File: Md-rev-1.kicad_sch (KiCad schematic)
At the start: 25 parts, among them CN1 JSTPH, J1 USB_C_Receptacle_USB2.0, J2 54-00177, U1 MCP73831-2-OT, U2 MAX9814

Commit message: updated gerberfiles and symbols
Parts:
- removed MK1: Microphone_Condensor, Buzzer_Beeper:MagneticBuzzer_Kobitone_254-EMB73-RO, symbol Device:Microphone_Condenser
- added MK1: CMA-4544PF-W, CMA-4544PF-W:MIC_CMA-4544PF-W, symbol CMA_4544PF_W:CMA-4544PF-W
- renumbered R10 to R9
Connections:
- net GND: now also MK1.1
- net at C5.1, R8.1: now also MK1.2
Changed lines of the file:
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@@
   (junction (at 158.75 121.92) (diameter 0) (color 0 0 0 0)
   )
+  (junction (at 215.9 128.27) (diameter 0) (color 0 0 0 0)
+  )
   (junction (at 347.98 119.38) (diameter 0) (color 0 0 0 0)
   )
@@
   )
   (junction (at 215.9 118.11) (diameter 0) (color 0 0 0 0)
-  )
-  (junction (at 215.9 128.27) (diameter 0) (color 0 0 0 0)
   )
   (no_connect (at 139.7 119.38))
@@
   (no_connect (at 345.44 121.92))
   (no_connect (at 347.98 116.84))
-  (no_connect (at 234.95 110.49))
+  (no_connect (at 233.68 110.49))
   (no_connect (at 345.44 124.46))
   (no_connect (at 351.79 114.3))
@@
     (stroke (width 0) (type default))
   )
-  (wire (pts (xy 196.85 128.27) (xy 199.39 128.27))
+  (wire (pts (xy 205.74 125.73) (xy 212.09 125.73))
     (stroke (width 0) (type default))
   )
@@
     (stroke (width 0) (type default))
   )
-  (wire (pts (xy 234.95 110.49) (xy 240.03 110.49))
+  (wire (pts (xy 233.68 110.49) (xy 240.03 110.49))
     (stroke (width 0) (type default))
   )
@@
     (stroke (width 0) (type default))
   )
+  (wire (pts (xy 215.9 128.27) (xy 215.9 132.08))
+    (stroke (width 0) (type default))
+  )
   (wire (pts (xy 92.71 88.9) (xy 100.33 88.9))
     (stroke (width 0) (type default))
@@
     (stroke (width 0) (type default))
   )
+  (wire (pts (xy 205.74 125.73) (xy 205.74 127))
+    (stroke (width 0) (type default))
+  )
   (wire (pts (xy 180.34 148.59) (xy 180.34 118.11))
     (stroke (width 0) (type default))
@@
     (stroke (width 0) (type default))
   )
-  (wire (pts (xy 209.55 128.27) (xy 215.9 128.27))
-    (stroke (width 0) (type default))
-  )
   (wire (pts (xy 92.71 120.65) (xy 115.57 120.65))
     (stroke (width 0) (type default))
@@
   )
   (wire (pts (xy 227.33 128.27) (xy 227.33 120.65))
+    (stroke (width 0) (type default))
+  )
+  (wire (pts (xy 205.74 132.08) (xy 215.9 132.08))
     (stroke (width 0) (type default))
   )
@@
     )
   )
-  (symbol (lib_id "Device:Microphone_Condenser") (at 204.47 128.27 270) (unit 1)
-    (in_bom yes) (on_board yes) (dnp no) (fields_autoplaced)
-    (property "Reference" "MK1" (at 205.1685 120.65 90)
-      (effects (font (size 1.27 1.27)))
-    )
-    (property "Value" "Microphone_Condensor" (at 205.1685 123.19 90)
-      (effects (font (size 1.27 1.27)))
-    )
-    (property "Footprint" "Buzzer_Beeper:MagneticBuzzer_Kobitone_254-EMB73-RO" (at 207.01 128.27 90)
-      (effects (font (size 1.27 1.27)) hide)
-    )
-    (property "Datasheet" "~" (at 207.01 128.27 90)
-      (effects (font (size 1.27 1.27)) hide)
-    )
-    (pin "1")
-    (pin "2")
-    (instances
-      (project "Md-rev-1"
-        (path "/34e1f0a2-75b5-46dc-b967-b4433c15cc45"
-          (reference "MK1") (unit 1)
-        )
-      )
-    )
-  )
   (symbol (lib_id "Device:C") (at 302.26 120.65 90) (unit 1)
     (in_bom yes) (on_board yes) (dnp no) (fields_autoplaced)
@@
   (symbol (lib_id "power:GND") (at 204.47 137.16 0) (unit 1)
     (in_bom yes) (on_board yes) (dnp no) (fields_autoplaced)
-    (property "Reference" "#PWR012" (at 204.47 143.51 0)
+    (property "Reference" "#PWR011" (at 204.47 143.51 0)
       (effects (font (size 1.27 1.27)) hide)
     )
@@
       (project "Md-rev-1"
         (path "/34e1f0a2-75b5-46dc-b967-b4433c15cc45"
-          (reference "#PWR012") (unit 1)
+          (reference "#PWR011") (unit 1)
         )
       )
@@
   (symbol (lib_id "3352T-1-201LF:3352T-1-201LF") (at 364.49 114.3 0) (unit 1)
     (in_bom yes) (on_board yes) (dnp no) (fields_autoplaced)
-    (property "Reference" "R10" (at 364.49 107.95 0)
+    (property "Reference" "R9" (at 364.49 107.95 0)
       (effects (font (size 1.27 1.27)))
     )
@@
       (project "Md-rev-1"
         (path "/34e1f0a2-75b5-46dc-b967-b4433c15cc45"
-          (reference "R10") (unit 1)
+          (reference "R9") (unit 1)
         )
       )
@@
   (symbol (lib_id "power:GND") (at 359.41 138.43 0) (unit 1)
     (in_bom yes) (on_board yes) (dnp no) (fields_autoplaced)
-    (property "Reference" "#PWR015" (at 359.41 144.78 0)
+    (property "Reference" "#PWR014" (at 359.41 144.78 0)
       (effects (font (size 1.27 1.27)) hide)
     )
@@
       (project "Md-rev-1"
         (path "/34e1f0a2-75b5-46dc-b967-b4433c15cc45"
-          (reference "#PWR015") (unit 1)
+          (reference "#PWR014") (unit 1)
         )
       )
@@
         (path "/34e1f0a2-75b5-46dc-b967-b4433c15cc45"
           (reference "#PWR04") (unit 1)
+        )
+      )
+    )
+  )
+  (symbol (lib_id "CMA_4544PF_W:CMA-4544PF-W") (at 198.12 129.54 0) (unit 1)
+    (in_bom yes) (on_board yes) (dnp no) (fields_autoplaced)
+    (property "Reference" "MK1" (at 199.39 121.92 0)
+      (effects (font (size 1.27 1.27)))
+    )
+    (property "Value" "CMA-4544PF-W" (at 199.39 124.46 0)
+      (effects (font (size 1.27 1.27)))
+    )
+    (property "Footprint" "CMA-4544PF-W:MIC_CMA-4544PF-W" (at 198.12 129.54 0)
+      (effects (font (size 1.27 1.27)) (justify bottom) hide)
+    )
+    (property "Datasheet" "" (at 198.12 129.54 0)
+      (effects (font (size 1.27 1.27)) hide)
+    )
+    (property "MF" "CUI Inc." (at 198.12 129.54 0)
+      (effects (font (size 1.27 1.27)) (justify bottom) hide)
+    )
+    (property "DESCRIPTION" "9.7 mm, Omnidirectional, PCB Mount, 3.0 Vdc, Electret Condenser Microphone" (at 198.12 129.54 0)
+      (effects (font (size 1.27 1.27)) (justify bottom) hide)
+    )
+    (property "PACKAGE" "6-DIP-6 CUI" (at 198.12 129.54 0)
+      (effects (font (size 1.27 1.27)) (justify bottom) hide)
+    )
+    (property "PRICE" "None" (at 198.12 129.54 0)
+      (effects (font (size 1.27 1.27)) (justify bottom) hide)
+    )
+    (property "CUI_PURCHASE_URL" "https://www.cui.com/product/audio/microphones/electret-condenser-microphones/cma-4544pf-w?utm_source=snapeda.com&utm_medium=referral&utm_campaign=snapedaBOM" (at 198.12 129.54 0)
+      (effects (font (size 1.27 1.27)) (justify bottom) hide)
+    )
+    (property "MP" "CMA-4544PF-W" (at 198.12 129.54 0)
+      (effects (font (size 1.27 1.27)) (justify bottom) hide)
+    )
+    (property "AVAILABILITY" "Unavailable" (at 198.12 129.54 0)
+      (effects (font (size 1.27 1.27)) (justify bottom) hide)
+    )
+    (pin "1")
+    (pin "2")
+    (instances
+      (project "Md-rev-1"
+        (path "/34e1f0a2-75b5-46dc-b967-b4433c15cc45"
+          (reference "MK1") (unit 1)
         )
       )
@@
     )
   )
-  (symbol (lib_id "power:GND") (at 196.85 128.27 0) (unit 1)
-    (in_bom yes) (on_board yes) (dnp no) (fields_autoplaced)
-    (property "Reference" "#PWR011" (at 196.85 134.62 0)
-      (effects (font (size 1.27 1.27)) hide)
-    )
-    (property "Value" "GND" (at 196.85 133.35 0)
-      (effects (font (size 1.27 1.27)))
-    )
-    (property "Footprint" "" (at 196.85 128.27 0)
-      (effects (font (size 1.27 1.27)) hide)
-    )
-    (property "Datasheet" "" (at 196.85 128.27 0)
-      (effects (font (size 1.27 1.27)) hide)
-    )
-    (pin "1")
-    (instances
-      (project "Md-rev-1"
-        (path "/34e1f0a2-75b5-46dc-b967-b4433c15cc45"
-          (reference "#PWR011") (unit 1)
-        )
-      )
+  (symbol (lib_id "power:GND") (at 212.09 125.73 0) (unit 1)
+    (in_bom yes) (on_board yes) (dnp no)
+    (property "Reference" "#PWR012" (at 212.09 132.08 0)
+      (effects (font (size 1.27 1.27)) hide)
+    )
+    (property "Value" "GND" (at 212.09 129.54 0)
+      (effects (font (size 1.27 1.27)))
+    )
+    (property "Footprint" "" (at 212.09 125.73 0)
+      (effects (font (size 1.27 1.27)) hide)
+    )
+    (property "Datasheet" "" (at 212.09 125.73 0)
+      (effects (font (size 1.27 1.27)) hide)
+    )
+    (pin "1")
+    (instances
+      (project "Md-rev-1"
+        (path "/34e1f0a2-75b5-46dc-b967-b4433c15cc45"
+          (reference "#PWR012") (unit 1)
+        )
+      )

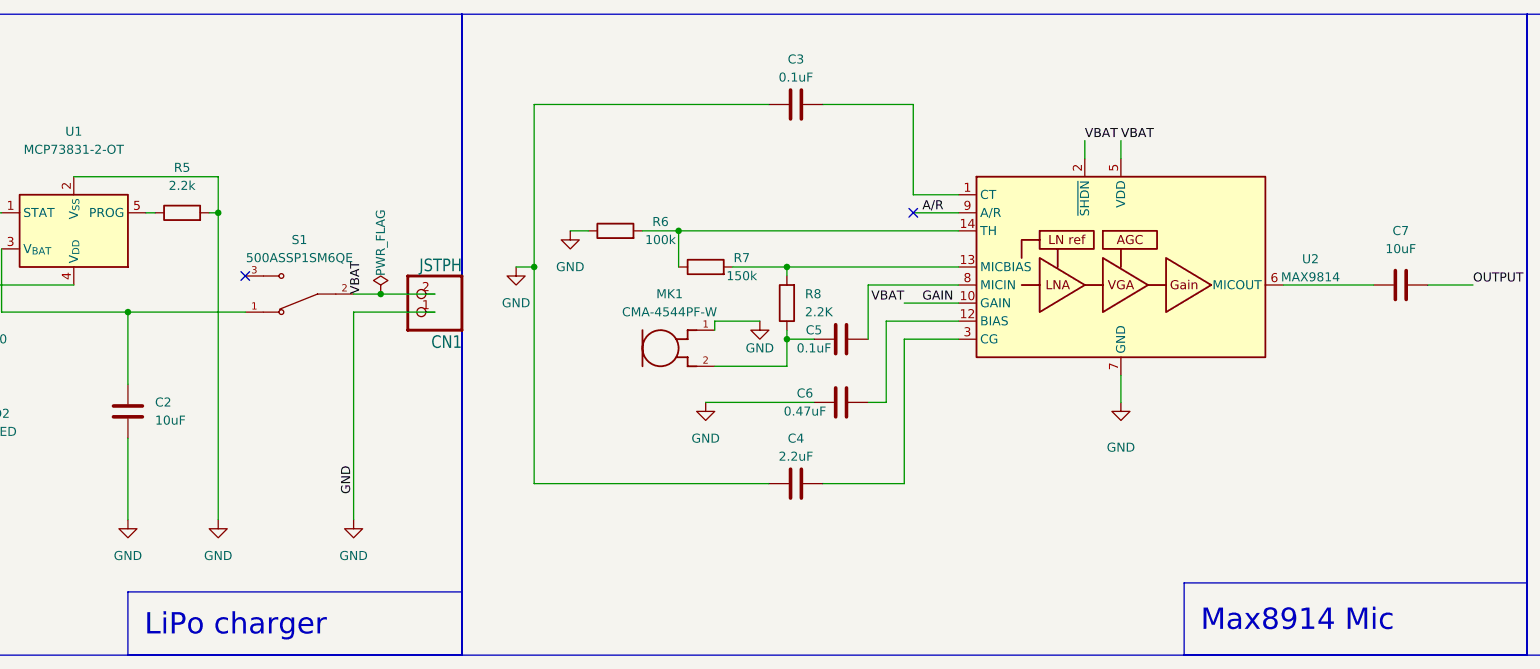
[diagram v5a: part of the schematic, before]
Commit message: Reorganized the board to meet some of the design rules listed from similar pcb's
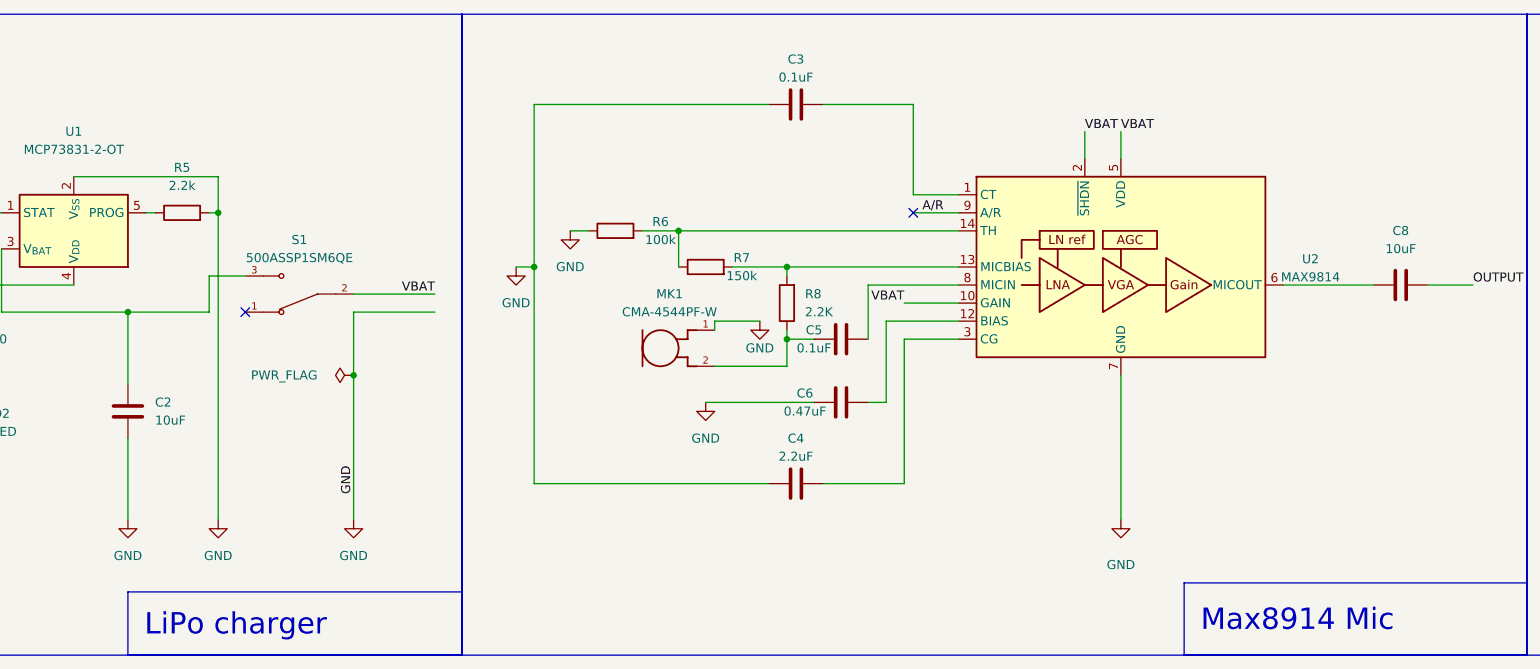
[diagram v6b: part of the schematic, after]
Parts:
- removed CN1: JSTPH, Connector_JST:JST_PH_S2B-PH-K_1x02_P2.00mm_Horizontal, symbol Adafruit USB C microlipo charger-eagle-import:JST_2PIN
- renumbered C7 to C8
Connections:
- net at C2.1, U1.3 (V_{BAT}): now also S1.3; no longer S1.1
- net GAIN renamed VBAT
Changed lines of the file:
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@@
   (junction (at 82.55 120.65) (diameter 0) (color 0 0 0 0)
   )
+  (junction (at 154.94 133.35) (diameter 0) (color 0 0 0 0)
+  )
   (junction (at 180.34 118.11) (diameter 0) (color 0 0 0 0)
   )
-  (junction (at 158.75 121.92) (diameter 0) (color 0 0 0 0)
-  )
   (junction (at 215.9 128.27) (diameter 0) (color 0 0 0 0)
   )
   (junction (at 347.98 119.38) (diameter 0) (color 0 0 0 0)
   )
+  (junction (at 34.29 148.59) (diameter 0) (color 0 0 0 0)
+  )
+  (junction (at 92.71 120.65) (diameter 0) (color 0 0 0 0)
+  )
   (junction (at 123.19 124.46) (diameter 0) (color 0 0 0 0)
   )
-  (junction (at 34.29 148.59) (diameter 0) (color 0 0 0 0)
-  )
-  (junction (at 92.71 120.65) (diameter 0) (color 0 0 0 0)
-  )
   (junction (at 100.33 110.49) (diameter 0) (color 0 0 0 0)
   )
@@
   (junction (at 215.9 118.11) (diameter 0) (color 0 0 0 0)
   )
-  (no_connect (at 139.7 119.38))
+  (no_connect (at 139.7 124.46))
   (no_connect (at 62.23 123.19))
   (no_connect (at 62.23 130.81))
@@
     (stroke (width 0) (type default))
   )
-  (wire (pts (xy 154.94 124.46) (xy 154.94 153.67))
+  (wire (pts (xy 154.94 124.46) (xy 154.94 133.35))
     (stroke (width 0) (type default))
   )
@@
     (stroke (width 0) (type default))
   )
-  (wire (pts (xy 257.81 100.33) (xy 257.81 102.87))
+  (wire (pts (xy 257.81 99.06) (xy 257.81 102.87))
     (stroke (width 0) (type default))
   )
@@
     (stroke (width 0) (type default))
   )
-  (wire (pts (xy 154.94 121.92) (xy 158.75 121.92))
-    (stroke (width 0) (type default))
-  )
   (wire (pts (xy 232.41 123.19) (xy 240.03 123.19))
     (stroke (width 0) (type default))
@@
     (stroke (width 0) (type default))
   )
-  (wire (pts (xy 262.89 100.33) (xy 262.89 102.87))
+  (wire (pts (xy 262.89 99.06) (xy 262.89 102.87))
+    (stroke (width 0) (type default))
+  )
+  (wire (pts (xy 134.62 124.46) (xy 134.62 119.38))
     (stroke (width 0) (type default))
   )
@@
     (stroke (width 0) (type default))
   )
+  (wire (pts (xy 205.74 132.08) (xy 215.9 132.08))
+    (stroke (width 0) (type default))
+  )
   (wire (pts (xy 92.71 120.65) (xy 115.57 120.65))
     (stroke (width 0) (type default))
@@
     (stroke (width 0) (type default))
   )
-  (wire (pts (xy 205.74 132.08) (xy 215.9 132.08))
-    (stroke (width 0) (type default))
-  )
   (wire (pts (xy 200.66 113.03) (xy 240.03 113.03))
     (stroke (width 0) (type default))
@@
     (stroke (width 0) (type default))
   )
-  (wire (pts (xy 123.19 124.46) (xy 139.7 124.46))
-    (stroke (width 0) (type default))
-  )
   (wire (pts (xy 220.98 95.25) (xy 233.68 95.25))
     (stroke (width 0) (type default))
@@
     (stroke (width 0) (type default))
   )
+  (wire (pts (xy 154.94 133.35) (xy 154.94 153.67))
+    (stroke (width 0) (type default))
+  )
   (wire (pts (xy 233.68 107.95) (xy 240.03 107.95))
     (stroke (width 0) (type default))
@@
     (stroke (width 0) (type default))
   )
-  (wire (pts (xy 262.89 133.35) (xy 262.89 137.16))
+  (wire (pts (xy 262.89 133.35) (xy 262.89 153.67))
+    (stroke (width 0) (type default))
+  )
+  (wire (pts (xy 123.19 124.46) (xy 134.62 124.46))
     (stroke (width 0) (type default))
   )
@@
     (stroke (width 0) (type default))
   )
-  (wire (pts (xy 158.75 121.92) (xy 166.37 121.92))
+  (wire (pts (xy 154.94 121.92) (xy 166.37 121.92))
     (stroke (width 0) (type default))
   )
   (wire (pts (xy 57.15 125.73) (xy 62.23 125.73))
+    (stroke (width 0) (type default))
+  )
+  (wire (pts (xy 134.62 119.38) (xy 139.7 119.38))
     (stroke (width 0) (type default))
   )
@@
     (effects (font (size 3 3)) (justify left top))
   )
-  (label "GAIN" (at 234.95 123.19 0) (fields_autoplaced)
-    (effects (font (size 1.27 1.27)) (justify left bottom))
-  )
   (label "VBAT" (at 232.41 123.19 180) (fields_autoplaced)
     (effects (font (size 1.27 1.27)) (justify right bottom))
   )
-  (label "VBAT" (at 156.21 121.92 90) (fields_autoplaced)
-    (effects (font (size 1.27 1.27)) (justify left bottom))
+  (label "VBAT" (at 166.37 121.92 180) (fields_autoplaced)
+    (effects (font (size 1.27 1.27)) (justify right bottom))
   )
   (label "OUTPUT" (at 312.42 120.65 0) (fields_autoplaced)
@@
     (effects (font (size 1.27 1.27)) (justify right bottom))
   )
-  (label "VBAT" (at 257.81 100.33 0) (fields_autoplaced)
+  (label "VBAT" (at 257.81 99.06 0) (fields_autoplaced)
     (effects (font (size 1.27 1.27)) (justify left bottom))
-    (property "VBAT" "" (at 257.81 101.6 0)
+    (property "VBAT" "" (at 257.81 100.33 0)
       (effects (font (size 1.27 1.27) italic) (justify left))
     )
   )
-  (label "VBAT" (at 262.89 100.33 0) (fields_autoplaced)
+  (label "VBAT" (at 262.89 99.06 0) (fields_autoplaced)
     (effects (font (size 1.27 1.27)) (justify left bottom))
-    (property "VBAT" "" (at 262.89 101.6 0)
+    (property "VBAT" "" (at 262.89 100.33 0)
       (effects (font (size 1.27 1.27) italic) (justify left))
     )
@@
     )
   )
-  (symbol (lib_id "power:PWR_FLAG") (at 158.75 121.92 0) (unit 1)
+  (symbol (lib_id "power:PWR_FLAG") (at 154.94 133.35 90) (unit 1)
     (in_bom yes) (on_board yes) (dnp no)
-    (property "Reference" "#FLG02" (at 158.75 120.015 0)
-      (effects (font (size 1.27 1.27)) hide)
-    )
-    (property "Value" "PWR_FLAG" (at 158.75 119.38 90)
+    (property "Reference" "#FLG02" (at 153.035 133.35 0)
+      (effects (font (size 1.27 1.27)) hide)
+    )
+    (property "Value" "PWR_FLAG" (at 149.86 133.35 90)
       (effects (font (size 1.27 1.27)) (justify left))
     )
-    (property "Footprint" "" (at 158.75 121.92 0)
-      (effects (font (size 1.27 1.27)) hide)
-    )
-    (property "Datasheet" "~" (at 158.75 121.92 0)
+    (property "Footprint" "" (at 154.94 133.35 0)
+      (effects (font (size 1.27 1.27)) hide)
+    )
+    (property "Datasheet" "~" (at 154.94 133.35 0)
       (effects (font (size 1.27 1.27)) hide)
     )
@@
   (symbol (lib_id "Device:C") (at 302.26 120.65 90) (unit 1)
     (in_bom yes) (on_board yes) (dnp no) (fields_autoplaced)
-    (property "Reference" "C7" (at 302.26 113.03 90)
+    (property "Reference" "C8" (at 302.26 113.03 90)
       (effects (font (size 1.27 1.27)))
     )
@@
       (project "Md-rev-1"
         (path "/34e1f0a2-75b5-46dc-b967-b4433c15cc45"
-          (reference "C7") (unit 1)
+          (reference "C8") (unit 1)
         )
       )
@@
     )
   )
+  (symbol (lib_id "power:GND") (at 262.89 153.67 0) (unit 1)
+    (in_bom yes) (on_board yes) (dnp no) (fields_autoplaced)
+    (property "Reference" "#PWR013" (at 262.89 160.02 0)
+      (effects (font (size 1.27 1.27)) hide)
+    )
+    (property "Value" "GND" (at 262.89 160.02 0)
+      (effects (font (size 1.27 1.27)))
+    )
+    (property "Footprint" "" (at 262.89 153.67 0)
+      (effects (font (size 1.27 1.27)) hide)
+    )
+    (property "Datasheet" "" (at 262.89 153.67 0)
+      (effects (font (size 1.27 1.27)) hide)
+    )
+    (pin "1")
+    (instances
+      (project "Md-rev-1"
+        (path "/34e1f0a2-75b5-46dc-b967-b4433c15cc45"
+          (reference "#PWR013") (unit 1)
+        )
+      )
+    )
+  )
   (symbol (lib_id "power:GND") (at 100.33 153.67 0) (unit 1)
     (in_bom yes) (on_board yes) (dnp no) (fields_autoplaced)
@@
     )
   )
-  (symbol (lib_id "Adafruit USB C microlipo charger-eagle-import:JST_2PIN") (at 163.83 121.92 180) (unit 1)
-    (in_bom yes) (on_board yes) (dnp no)
-    (property "Reference" "CN1" (at 170.18 127.635 0)
-      (effects (font (size 1.778 1.5113)) (justify left bottom))
-    )
-    (property "Value" "JSTPH" (at 170.18 116.84 0)
-      (effects (font (size 1.778 1.5113)) (justify left bottom))
-    )
-    (property "Footprint" "Connector_JST:JST_PH_S2B-PH-K_1x02_P2.00mm_Horizontal" (at 163.83 121.92 0)
-      (effects (font (size 1.27 1.27)) hide)
-    )
-    (property "Datasheet" "" (at 163.83 121.92 0)
-      (effects (font (size 1.27 1.27)) hide)
-    )
-    (pin "1")
-    (pin "2")
-    (instances
-      (project "Mn-dev"
-        (path "/09bb9ecc-23a0-4cc1-ac3b-f2e74c0523fc"
-          (reference "CN1") (unit 1)
-        )
-      )
-      (project "Md-rev-1"
-        (path "/34e1f0a2-75b5-46dc-b967-b4433c15cc45"
-          (reference "CN1") (unit 1)
-        )
-      )
-      (project "Adafruit USB C microlipo charger"
-        (path "/e9aa8fe5-1b1b-4419-ba77-127f5be135ca"
-          (reference "CN2") (unit 1)
-        )
-      )
-    )
-  )
   (symbol (lib_id "Device:R") (at 130.81 110.49 90) (unit 1)
     (in_bom yes) (on_board yes) (dnp no) (fields_autoplaced)
@@
         )
       )
-    )
-  )
-  (symbol (lib_id "power:GND") (at 262.89 137.16 0) (unit 1)
-    (in_bom yes) (on_board yes) (dnp no) (fields_autoplaced)
-    (property "Reference" "#PWR013" (at 262.89 143.51 0)
-      (effects (font (size 1.27 1.27)) hide)
-    )
-    (property "Value" "GND" (at 262.89 143.51 0)
-      (effects (font (size 1.27 1.27)))
-    )
-    (property "Footprint" "" (at 262.89 137.16 0)
-      (effects (font (size 1.27 1.27)) hide)
-    )
-    (property "Datasheet" "" (at 262.89 137.16 0)
-      (effects (font (size 1.27 1.27)) hide)
-    )
-    (pin "1")
-    (instances
-      (project "Md-rev-1"
-        (path "/34e1f0a2-75b5-46dc-b967-b4433c15cc45"
-          (reference "#PWR013") (unit 1)
-        )
-      )
